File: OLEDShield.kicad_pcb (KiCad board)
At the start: 2 copper layers, 68.6 x 53.3 mm, 290 parts, among them P1 CONN_5X2, P2 CONN_5X2, P3 CONN_1, P4 CONN_1, P5 CONN_1

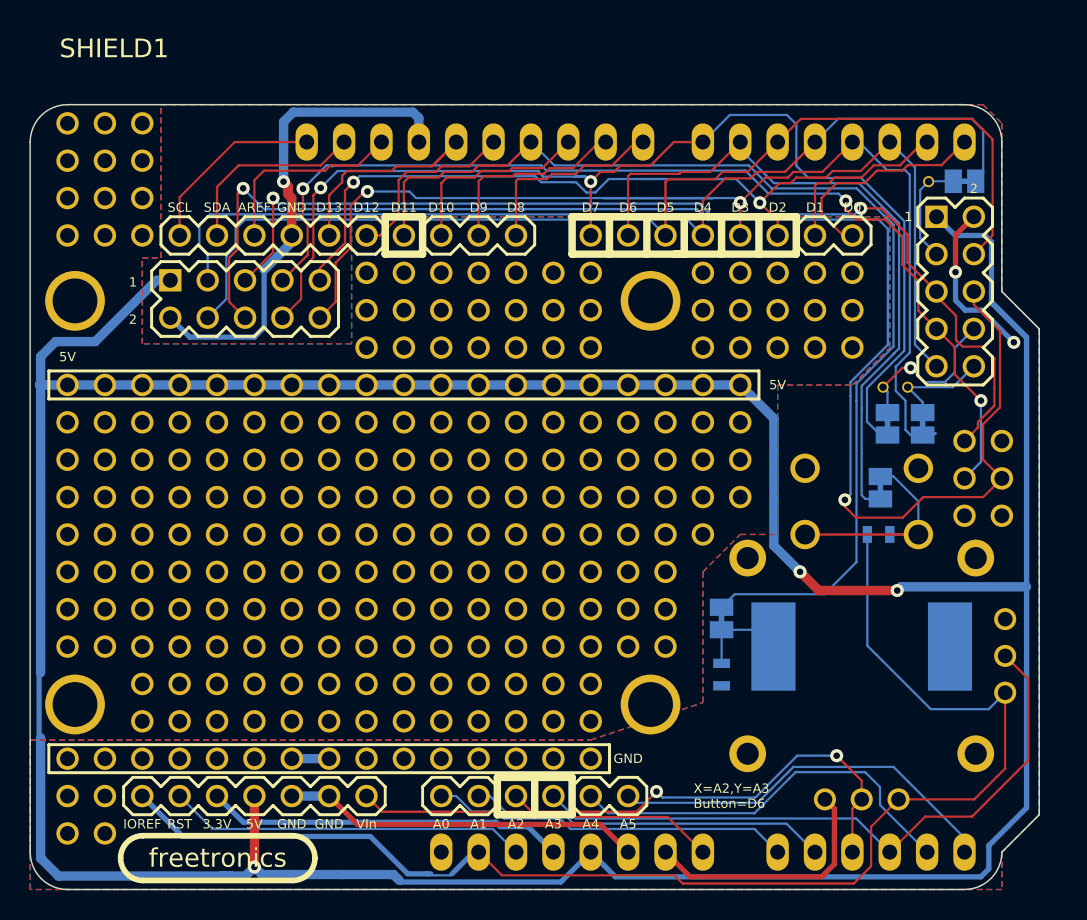
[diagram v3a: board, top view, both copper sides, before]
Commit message: Add ground pour in prototyping area, fix board edges to clear Ethernet jack, finish silkscreening
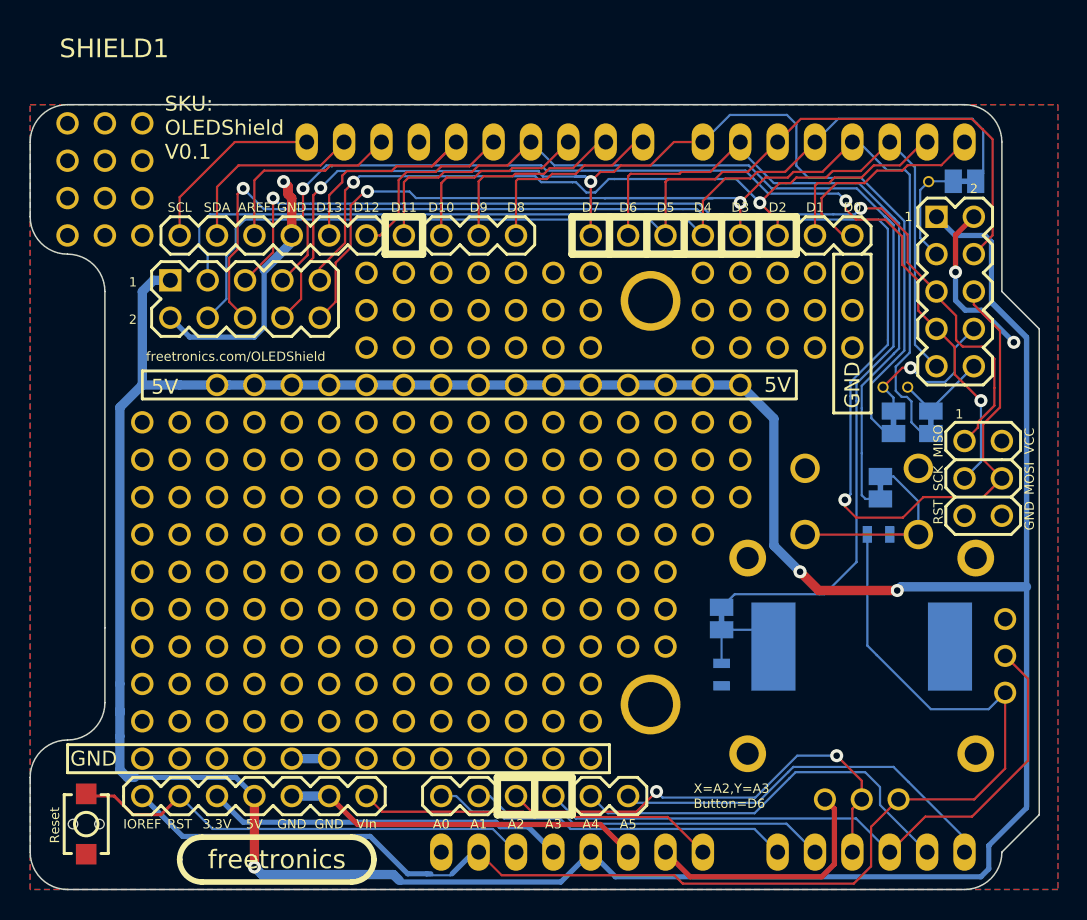
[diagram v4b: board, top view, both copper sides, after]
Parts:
- removed the 1PIN at (223.5, 247.7)
- removed the 1PIN at (221.0, 247.7)
- removed the 1PIN at (221.0, 245.1)
- removed the 1PIN at (223.5, 245.1)
- removed the 1PIN at (228.6, 242.6)
- removed the 1PIN at (223.5, 242.6)
- removed the 1PIN at (221.0, 242.6)
- removed the 1PIN at (226.1, 242.6)
- removed the 1PIN at (221.5, 236.9)
- removed the 1PIN at (221.5, 264.3)
- removed the 1PIN at (221.0, 250.2)
- removed the 1PIN at (223.5, 250.2)
- removed the 1PIN at (223.5, 252.7)
- removed the 1PIN at (221.0, 252.7)
- removed the 1PIN at (221.0, 255.3)
- removed the 1PIN at (223.5, 255.3)
- removed the 1PIN at (221.0, 270.5)
- removed the 1PIN at (223.5, 270.5)
- removed the 1PIN at (223.5, 273.1)
- removed the 1PIN at (221.0, 273.1)
- removed the 1PIN at (223.5, 268.0)
- removed the 1PIN at (221.0, 268.0)
- removed the 1PIN at (223.5, 260.4)
- removed the 1PIN at (221.0, 260.4)
- removed the 1PIN at (221.0, 257.8)
- removed the 1PIN at (223.5, 257.8)
- removed the ? at (231.2, 274.7)
- added SW1: SW_PUSHBUTTON, TACTILE_SWITCH_SMD_2PIN_TINY, F.Cu at (222.2, 272.4)
- moved ? 4.01 mm to (235.2, 274.8)
- moved SJ5 0.57 mm to (279.7, 245.1)
- moved SJ4 0.42 mm to (277.1, 245.1)
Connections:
- 1PIN pad 1: (no net) -> GND (x3)
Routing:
- net +5V: track 295.7 -> 273.3 mm
- net GND: track 106.5 -> 91.1 mm
- net /RST: track 24.4 -> 31.9 mm
- net /OLED_nRST: track 81.0 -> 79.3 mm
- net /RHS_OLED_nRST: track 7.23 -> 6.54 mm
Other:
- outline, holes or cut-outs redrawn
- rule pad_to_mask_clearance: 0 -> 0.1016
- board text added: "MISO"
- board text added: "MOSI"
- board text added: "OLED Shield by Angus Gratton (C) 2013 Freetronics Pty Ltd - TAPR OHL"
- board text added: "Reset"
- board text added: "SCK"
- board text added: "SKU: OLEDShield V0.1"
- board text added: "VCC"
- board text added: "freetronics.com/OLEDShield"

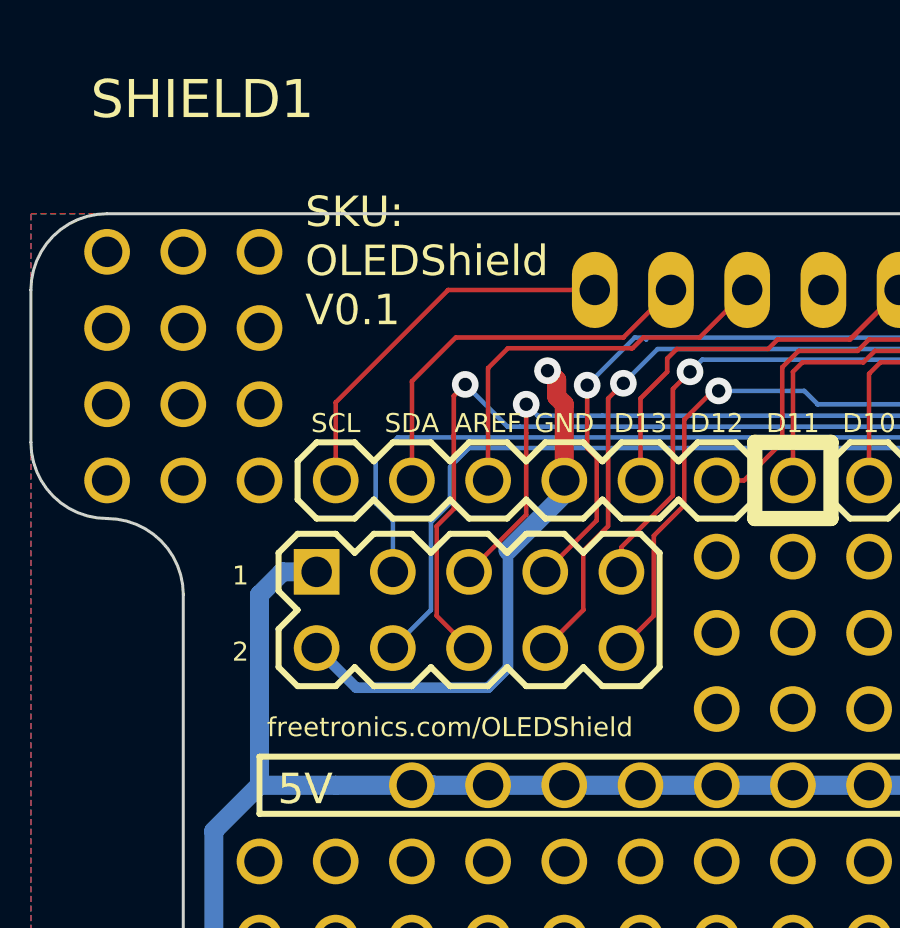
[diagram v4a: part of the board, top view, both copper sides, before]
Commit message: Fix URL, SKU capitalisation
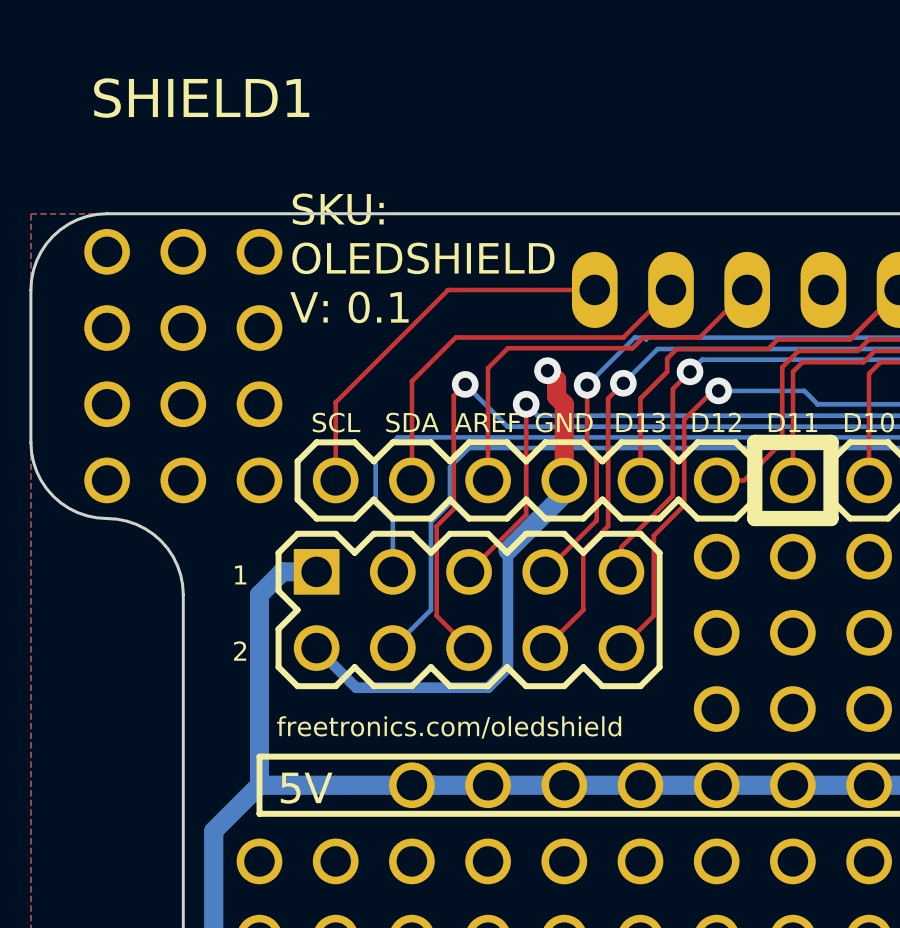
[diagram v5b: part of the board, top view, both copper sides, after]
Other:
- board text added: "SKU: OLEDSHIELD V: 0.1"
- board text added: "freetronics.com/oledshield"
- board text removed: "SKU: OLEDShield V0.1"
- board text removed: "freetronics.com/OLEDShield"
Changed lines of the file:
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@@
     (area 216.391067 218.5924 288.290001 277.3132)
     (thickness 1.6)
-    (drawings 563)
+    (drawings 564)
     (tracks 615)
     (zones 0)
@@
     )
   )
+  (gr_text "SKU:\nOLEDSHIELD\n      V: 0.1" (at 236.22 225.044) (layer B.SilkS)
+    (effects (font (size 1.016 1.016) (thickness 0.254)) (justify left mirror))
+  )
   (gr_text GND (at 286.3596 251.46 90) (layer F.SilkS)
     (effects (font (size 0.635 0.635) (thickness 0.15875)))
@@
   (gr_line (start 273.05 244.602) (end 275.59 244.602) (angle 90) (layer B.SilkS) (width 0.2))
   (gr_line (start 273.05 233.68) (end 273.05 244.602) (angle 90) (layer B.SilkS) (width 0.2))
-  (gr_text freetronics.com/OLEDShield (at 232.41 240.6396) (layer F.SilkS)
+  (gr_text freetronics.com/oledshield (at 232.41 240.6396) (layer F.SilkS)
     (effects (font (size 0.635 0.635) (thickness 0.15875)))
   )
-  (gr_text freetronics.com/OLEDShield (at 232.41 240.6396) (layer B.SilkS)
+  (gr_text freetronics.com/oledshield (at 232.41 240.6396) (layer B.SilkS)
     (effects (font (size 0.635 0.635) (thickness 0.15875)) (justify mirror))
   )
@@
     (effects (font (size 0.635 0.635) (thickness 0.15875)) (justify left mirror))
   )
-  (gr_text "SKU:\nOLEDShield\nV0.1" (at 227.584 225.0948) (layer F.SilkS)
+  (gr_text "SKU:\nOLEDSHIELD\nV: 0.1" (at 227.076 225.044) (layer F.SilkS)
     (effects (font (size 1.016 1.016) (thickness 0.254)) (justify left))
   )

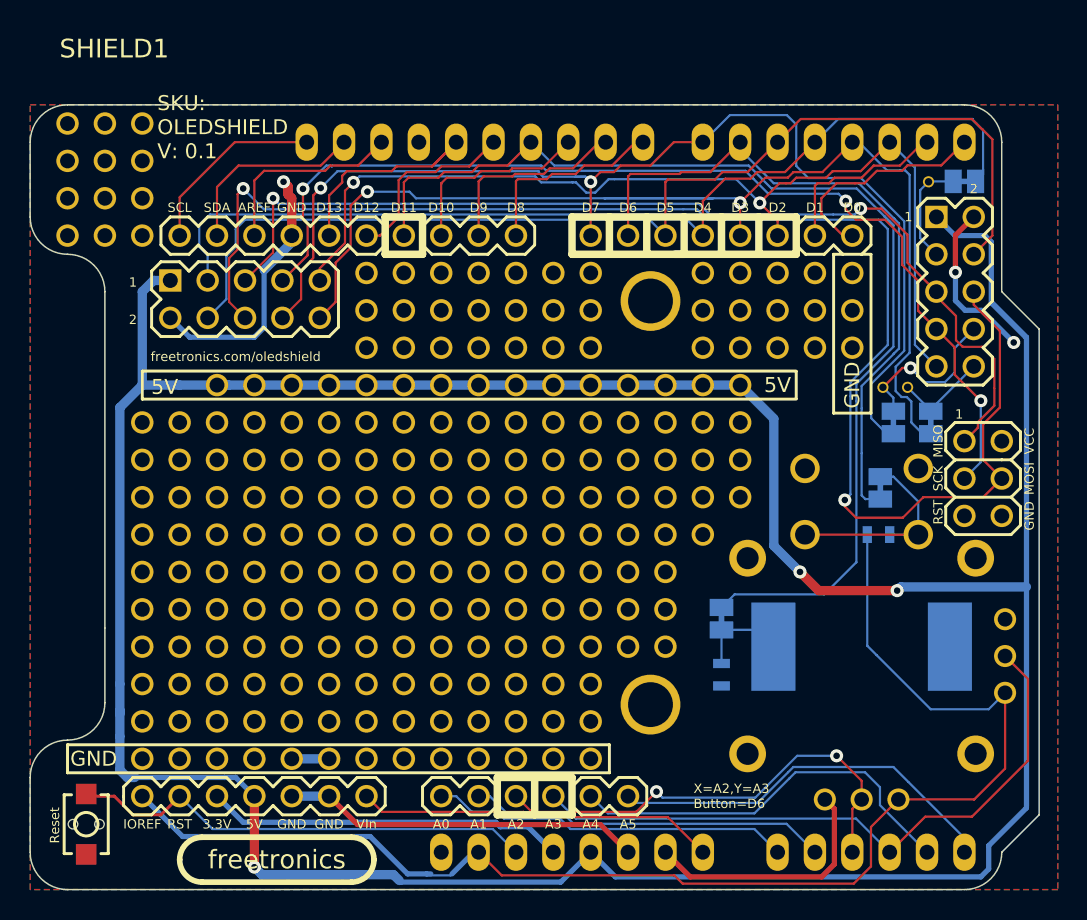
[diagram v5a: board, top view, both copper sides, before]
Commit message: Widen tracks where they connect to PTH pads
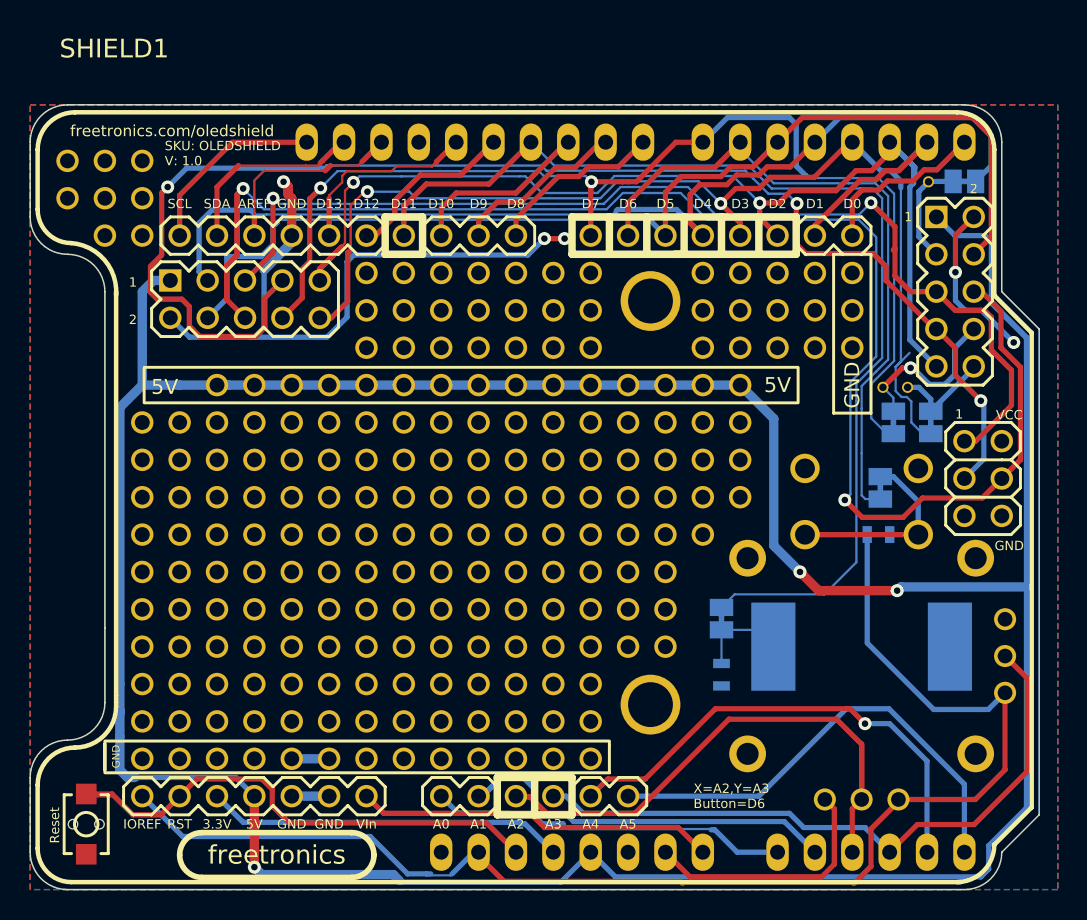
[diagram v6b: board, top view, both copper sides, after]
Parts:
- removed the 1PIN at (221.0, 232.4)
- removed the 1PIN at (226.1, 224.8)
- removed the 1PIN at (223.5, 224.8)
- removed the 1PIN at (221.0, 224.8)
- moved ? 0.32 mm to (235.2, 274.5)
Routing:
- net /SCK: track 70.0 -> 93.9 mm
- net /MOSI: track 101.2 -> 110.8 mm
- net /AD2_JOY_X: track 31.7 -> 39.6 mm, vias 2 -> 0
- net /MISO: track 69.0 -> 76.7 mm
- net /RST: track 31.9 -> 39.2 mm
- net /AD1: track 24.4 -> 31.6 mm
- net /OLED_DnC: track 66.7 -> 72.9 mm
- net /OLED_nRST: track 79.3 -> 73.7 mm
- net /AD4: track 27.5 -> 33.0 mm, vias 0 -> 1
- net /AD5: track 27.0 -> 32.1 mm
- net GND: track 91.1 -> 95.6 mm, vias 3 -> 5
- net /OLED_nCS: track 77.5 -> 81.1 mm
- net /AD0: track 24.4 -> 27.9 mm
- net /D0: track 15.1 -> 11.7 mm
- net N-0000038: track 15.2 -> 18.5 mm
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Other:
- board text added: "SKU: OLEDSHIELD V: 1.0"
- board text removed: "MISO"
- board text removed: "MOSI"
- board text removed: "SCK"
- board text removed: "SKU: OLEDSHIELD V: 0.1"

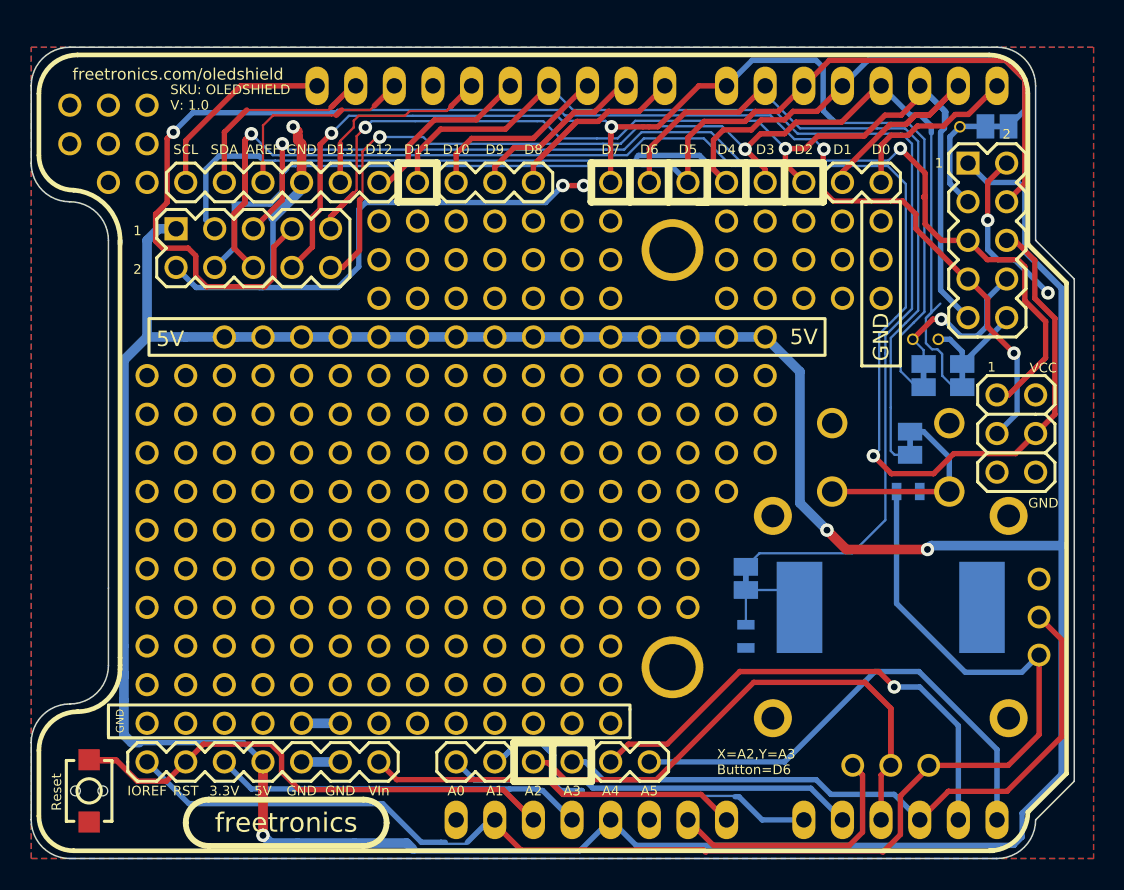
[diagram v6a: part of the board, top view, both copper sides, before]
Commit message: Reroute board with joystick footprint correctly oriented
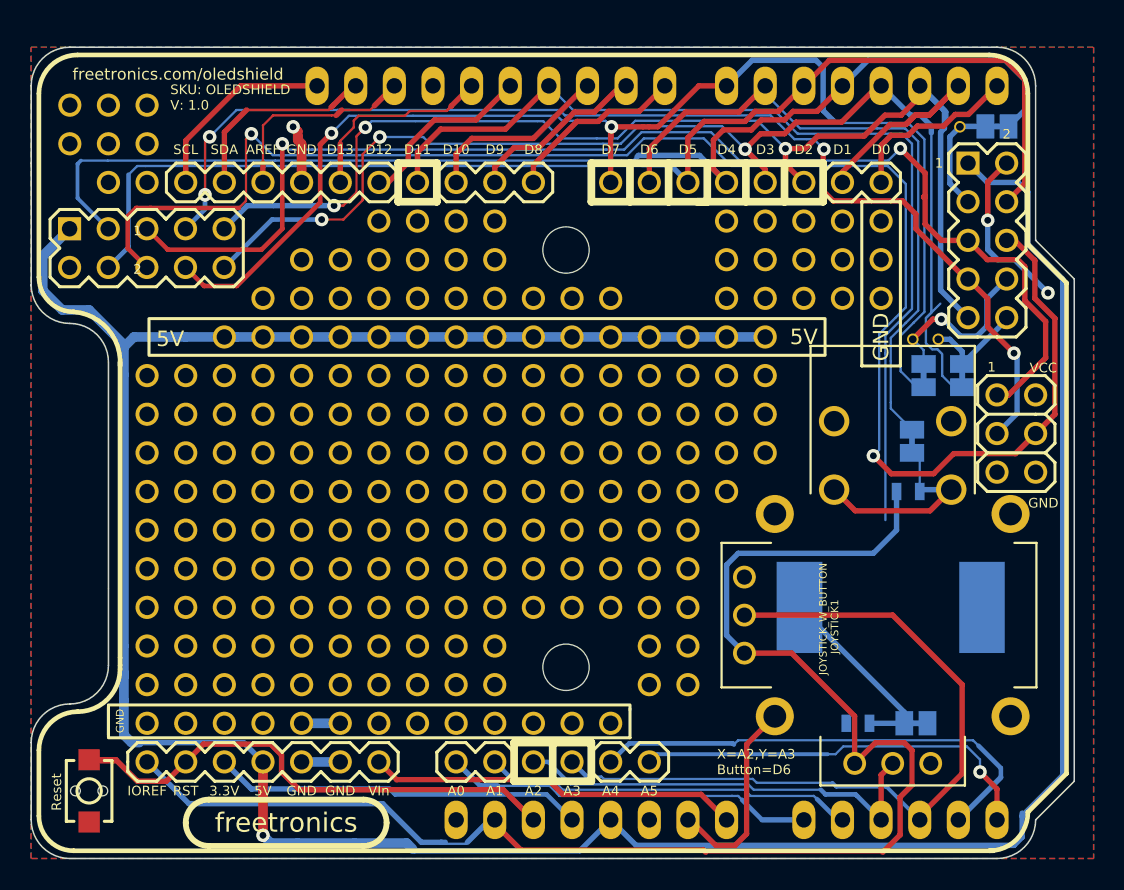
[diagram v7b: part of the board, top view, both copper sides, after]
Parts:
- removed the 1PIN at (251.5, 234.9)
- removed the 1PIN at (254.0, 234.9)
- removed the 1PIN at (256.5, 234.9)
- removed the 1PIN at (251.5, 237.5)
- removed the 1PIN at (254.0, 237.5)
- removed the 1PIN at (256.5, 237.5)
- removed the 1PIN at (256.5, 265.4)
- removed the 1PIN at (256.5, 262.9)
- removed the 1PIN at (254.0, 262.9)
- removed the 1PIN at (251.5, 262.9)
- removed the 1PIN at (251.5, 265.4)
- removed the 1PIN at (254.0, 265.4)
- added 1PIN: P***, 1pin_prototyping, F.Cu at (261.6, 262.9)
- added 1PIN: P***, 1pin_prototyping, F.Cu at (261.6, 265.4)
- added 1PIN: P***, 1pin_prototyping, F.Cu at (259.1, 265.4)
- added 1PIN: P***, 1pin_prototyping, F.Cu at (259.1, 262.9)
- added 1PIN: P***, 1pin_prototyping, F.Cu at (233.7, 240.0)
- added 1PIN: P***, 1pin_prototyping, F.Cu at (236.2, 237.5)
- added 1PIN: P***, 1pin_prototyping, F.Cu at (236.2, 240.0)
- added 1PIN: P***, 1pin_prototyping, F.Cu at (238.8, 240.0)
- added 1PIN: P***, 1pin_prototyping, F.Cu at (238.8, 237.5)
- JOYSTICK1: moved to F.Cu
- moved SJ1 14.7 mm to (276.6, 268.0), turned to 180 degrees
- moved R1 9.32 mm to (272.8, 268.0), turned to 0 degrees
- moved P1 7.00 mm to (221.0, 235.5)
- moved 1PIN 7.00 mm to (253.6, 264.3)
- moved 1PIN 7.00 mm to (253.6, 236.9)
- moved JOYSTICK1 0.18 mm to (275.1, 260.9)
- moved SJ2 0.18 mm to (276.4, 249.4), turned to 270 degrees
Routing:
- net +5V: track 273.3 -> 203.1 mm, vias 3 -> 1
- net GND: track 95.6 -> 39.3 mm, vias 5 -> 3
- net /SCK: track 93.9 -> 77.0 mm, vias 3 -> 4
- net /D11: track 73.8 -> 63.3 mm
- net /AD2_JOY_X: track 39.6 -> 29.2 mm
- net /uSD_nCS: track 69.6 -> 78.6 mm
- net /uSD_CD: track 76.5 -> 83.8 mm
- net /OLED_nCS: track 81.1 -> 87.7 mm
- net /MISO: track 76.7 -> 83.2 mm
- net N-0000011: track 6.28 -> 12.8 mm
- net /AD3_JOY_Y: track 44.5 -> 50.7 mm
- net VCC: track 93.6 -> 99.4 mm
- net /OLED_nRST: track 73.7 -> 79.1 mm, vias 2 -> 3
- net /AD1: track 31.6 -> 26.4 mm
- net /AD5: track 32.1 -> 26.9 mm, vias 0 -> 1
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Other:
- outline, holes or cut-outs redrawn
